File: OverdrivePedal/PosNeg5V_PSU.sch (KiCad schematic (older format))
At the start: 19 parts, among them Q1 DMG2301L, U2 TC7662Bx0A, U3 MIC5233YM5, U4 MIC5270YM5

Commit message: RevA Layout completed
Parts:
- C10, C11, C3, C6, C8: footprint Capacitor_SMD:C_1206_3216Metric_Pad1.42x1.75mm_HandSolder -> Capacitor_SMD:C_0805_2012Metric_Pad1.15x1.40mm_HandSolder
- D1: footprint Diode_SMD:D_SOD-123F -> Diode_SMD:D_SOD-323_HandSoldering
- R4, R5, R6, R7, R8: footprint Resistor_SMD:R_1206_3216Metric_Pad1.42x1.75mm_HandSolder -> Resistor_SMD:R_0805_2012Metric_Pad1.15x1.40mm_HandSolder
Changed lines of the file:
@@
 F 0 "D1" V 3004 2179 50  0000 L CNN
 F 1 "10V" V 3095 2179 50  0000 L CNN
-F 2 "Diode_SMD:D_SOD-123F" H 3050 2100 50  0001 C CNN
+F 2 "Diode_SMD:D_SOD-323_HandSoldering" H 3050 2100 50  0001 C CNN
 F 3 "~" H 3050 2100 50  0001 C CNN
 	1    3050 2100
@@
 F 0 "R4" H 2620 2596 50  0000 L CNN
 F 1 "100K" H 2620 2505 50  0000 L CNN
-F 2 "Resistor_SMD:R_1206_3216Metric_Pad1.42x1.75mm_HandSolder" V 2480 2550 50  0001 C CNN
+F 2 "Resistor_SMD:R_0805_2012Metric_Pad1.15x1.40mm_HandSolder" V 2480 2550 50  0001 C CNN
 F 3 "~" H 2550 2550 50  0001 C CNN
 	1    2550 2550
@@
 F 0 "R7" H 7170 2146 50  0000 L CNN
 F 1 "330R" H 7170 2055 50  0000 L CNN
-F 2 "Resistor_SMD:R_1206_3216Metric_Pad1.42x1.75mm_HandSolder" V 7030 2100 50  0001 C CNN
+F 2 "Resistor_SMD:R_0805_2012Metric_Pad1.15x1.40mm_HandSolder" V 7030 2100 50  0001 C CNN
 F 3 "~" H 7100 2100 50  0001 C CNN
 	1    7100 2100
@@
 F 0 "R5" H 7170 2796 50  0000 L CNN
 F 1 "1K" H 7170 2705 50  0000 L CNN
-F 2 "Resistor_SMD:R_1206_3216Metric_Pad1.42x1.75mm_HandSolder" V 7030 2750 50  0001 C CNN
+F 2 "Resistor_SMD:R_0805_2012Metric_Pad1.15x1.40mm_HandSolder" V 7030 2750 50  0001 C CNN
 F 3 "~" H 7100 2750 50  0001 C CNN
 	1    7100 2750
@@
 F 0 "C6" H 5315 2546 50  0000 L CNN
 F 1 "1uF" H 5315 2455 50  0000 L CNN
-F 2 "Capacitor_SMD:C_1206_3216Metric_Pad1.42x1.75mm_HandSolder" H 5238 2350 50  0001 C CNN
+F 2 "Capacitor_SMD:C_0805_2012Metric_Pad1.15x1.40mm_HandSolder" H 5238 2350 50  0001 C CNN
 F 3 "~" H 5200 2500 50  0001 C CNN
 	1    5200 2500
@@
 F 0 "C8" H 7585 2546 50  0000 R CNN
 F 1 "2.2uF" H 7585 2455 50  0000 R CNN
-F 2 "Capacitor_SMD:C_1206_3216Metric_Pad1.42x1.75mm_HandSolder" H 7738 2350 50  0001 C CNN
+F 2 "Capacitor_SMD:C_0805_2012Metric_Pad1.15x1.40mm_HandSolder" H 7738 2350 50  0001 C CNN
 F 3 "~" H 7700 2500 50  0001 C CNN
 	1    7700 2500
@@
 F 0 "R8" H 7170 4496 50  0000 L CNN
 F 1 "330R" H 7170 4405 50  0000 L CNN
-F 2 "Resistor_SMD:R_1206_3216Metric_Pad1.42x1.75mm_HandSolder" V 7030 4450 50  0001 C CNN
+F 2 "Resistor_SMD:R_0805_2012Metric_Pad1.15x1.40mm_HandSolder" V 7030 4450 50  0001 C CNN
 F 3 "~" H 7100 4450 50  0001 C CNN
 	1    7100 4450
@@
 F 0 "R6" H 7170 5096 50  0000 L CNN
 F 1 "1K" H 7170 5005 50  0000 L CNN
-F 2 "Resistor_SMD:R_1206_3216Metric_Pad1.42x1.75mm_HandSolder" V 7030 5050 50  0001 C CNN
+F 2 "Resistor_SMD:R_0805_2012Metric_Pad1.15x1.40mm_HandSolder" V 7030 5050 50  0001 C CNN
 F 3 "~" H 7100 5050 50  0001 C CNN
 	1    7100 5050
@@
 F 0 "C3" H 1665 4896 50  0000 L CNN
 F 1 "100nF" H 1665 4805 50  0000 L CNN
-F 2 "Capacitor_SMD:C_1206_3216Metric_Pad1.42x1.75mm_HandSolder" H 1588 4700 50  0001 C CNN
+F 2 "Capacitor_SMD:C_0805_2012Metric_Pad1.15x1.40mm_HandSolder" H 1588 4700 50  0001 C CNN
 F 3 "~" H 1550 4850 50  0001 C CNN
 	1    1550 4850
@@
 F 0 "C10" H 9615 2346 50  0000 L CNN
 F 1 "100nF" H 9615 2255 50  0000 L CNN
-F 2 "Capacitor_SMD:C_1206_3216Metric_Pad1.42x1.75mm_HandSolder" H 9538 2150 50  0001 C CNN
+F 2 "Capacitor_SMD:C_0805_2012Metric_Pad1.15x1.40mm_HandSolder" H 9538 2150 50  0001 C CNN
 F 3 "~" H 9500 2300 50  0001 C CNN
 	1    9500 2300
@@
 F 0 "C11" H 9565 4696 50  0000 L CNN
 F 1 "100nF" H 9565 4605 50  0000 L CNN
-F 2 "Capacitor_SMD:C_1206_3216Metric_Pad1.42x1.75mm_HandSolder" H 9488 4500 50  0001 C CNN
+F 2 "Capacitor_SMD:C_0805_2012Metric_Pad1.15x1.40mm_HandSolder" H 9488 4500 50  0001 C CNN
 F 3 "~" H 9450 4650 50  0001 C CNN
 	1    9450 4650

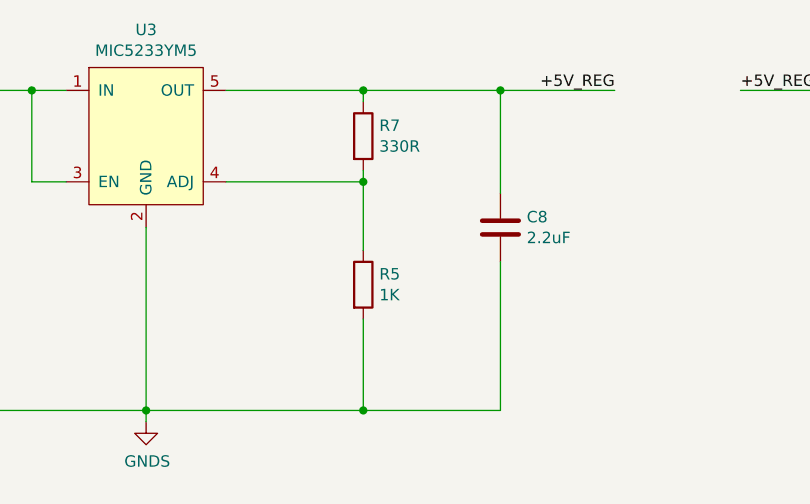
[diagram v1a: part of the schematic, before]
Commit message: Tested RevA Layout
- Removed AC coupling caps
- Reversed Switch connector
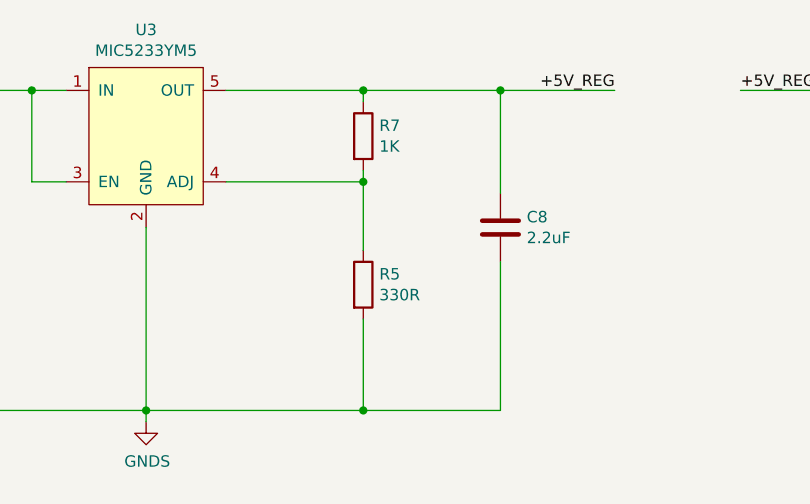
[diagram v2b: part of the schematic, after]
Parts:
- R5: value 1K -> 330R
- R7: value 330R -> 1K
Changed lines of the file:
@@
 AR Path="/5E6A8284/5E61A3C3" Ref="R?"  Part="1"
 F 0 "R7" H 7170 2146 50  0000 L CNN
-F 1 "330R" H 7170 2055 50  0000 L CNN
+F 1 "1K" H 7170 2055 50  0000 L CNN
 F 2 "Resistor_SMD:R_0805_2012Metric_Pad1.15x1.40mm_HandSolder" V 7030 2100 50  0001 C CNN
 F 3 "~" H 7100 2100 50  0001 C CNN
@@
 AR Path="/5E6A8284/5E61A7F8" Ref="R?"  Part="1"
 F 0 "R5" H 7170 2796 50  0000 L CNN
-F 1 "1K" H 7170 2705 50  0000 L CNN
+F 1 "330R" H 7170 2705 50  0000 L CNN
 F 2 "Resistor_SMD:R_0805_2012Metric_Pad1.15x1.40mm_HandSolder" V 7030 2750 50  0001 C CNN
 F 3 "~" H 7100 2750 50  0001 C CNN

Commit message: changed polarity protection mosfet to schotky diode
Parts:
- removed D1: 10V, Diode_SMD:D_SOD-323_HandSoldering, symbol Device:D_Zener
- removed Q1: DMG2301L, Package_TO_SOT_SMD:SOT-23, symbol Transistor_FET:DMG2301L
- removed R4: 100K, Resistor_SMD:R_0805_2012Metric_Pad1.15x1.40mm_HandSolder, symbol Device:R
- added D1: D_Schottky, Diode_SMD:D_SOD-123F, symbol Device:D_Schottky
- U2: symbol Converter_DCDC:TC7662Bx0A -> OverdrivePedal-rescue:TC7662Bx0A-Converter_DCDC
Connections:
- net +9V_IN: now also D1.2 (A)
- net +9V_POL: now also D1.1 (K)
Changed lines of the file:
@@
 $EndDescr
 $Comp
-L Converter_DCDC:TC7662Bx0A U?
+L OverdrivePedal-rescue:TC7662Bx0A-Converter_DCDC U?
 U 1 1 5E618EFD
 P 2450 4500
@@
 	1    0    0    -1
 $EndComp
-$Comp
-L Transistor_FET:DMG2301L Q?
-U 1 1 5E618F03
-P 2550 2000
-AR Path="/5E618F03" Ref="Q?"  Part="1"
-AR Path="/5E6165F4/5E618F03" Ref="Q1"  Part="1"
-AR Path="/5E6A8284/5E618F03" Ref="Q?"  Part="1"
-F 0 "Q1" V 2892 2000 50  0000 C CNN
-F 1 "DMG2301L" V 2801 2000 50  0000 C CNN
-F 2 "Package_TO_SOT_SMD:SOT-23" H 2750 1925 50  0001 L CIN
-F 3 "https://www.diodes.com/assets/Datasheets/DMG2301L.pdf" H 2550 2000 50  0001 L CNN
-	1    2550 2000
-	0    -1   -1   0
-$EndComp
-$Comp
-L Device:D_Zener D?
-U 1 1 5E618F09
-P 3050 2100
-AR Path="/5E618F09" Ref="D?"  Part="1"
-AR Path="/5E6165F4/5E618F09" Ref="D1"  Part="1"
-AR Path="/5E6A8284/5E618F09" Ref="D?"  Part="1"
-F 0 "D1" V 3004 2179 50  0000 L CNN
-F 1 "10V" V 3095 2179 50  0000 L CNN
-F 2 "Diode_SMD:D_SOD-323_HandSoldering" H 3050 2100 50  0001 C CNN
-F 3 "~" H 3050 2100 50  0001 C CNN
-	1    3050 2100
-	0    1    1    0
-$EndComp
-$Comp
-L Device:R R?
-U 1 1 5E618F0F
-P 2550 2550
-AR Path="/5E618F0F" Ref="R?"  Part="1"
-AR Path="/5E6165F4/5E618F0F" Ref="R4"  Part="1"
-AR Path="/5E6A8284/5E618F0F" Ref="R?"  Part="1"
-F 0 "R4" H 2620 2596 50  0000 L CNN
-F 1 "100K" H 2620 2505 50  0000 L CNN
-F 2 "Resistor_SMD:R_0805_2012Metric_Pad1.15x1.40mm_HandSolder" V 2480 2550 50  0001 C CNN
-F 3 "~" H 2550 2550 50  0001 C CNN
-	1    2550 2550
-	1    0    0    -1
-$EndComp
-Wire Wire Line
-	3050 1950 3050 1900
-Wire Wire Line
-	3050 1900 2750 1900
-Wire Wire Line
-	2550 2200 2550 2300
-Wire Wire Line
-	2550 2300 3050 2300
-Wire Wire Line
-	3050 2300 3050 2250
-Connection ~ 2550 2300
-Wire Wire Line
-	2550 2300 2550 2400
-$Comp
-L power:GNDS #PWR?
-U 1 1 5E618F1D
-P 2550 2850
-AR Path="/5E618F1D" Ref="#PWR?"  Part="1"
-AR Path="/5E6165F4/5E618F1D" Ref="#PWR012"  Part="1"
-AR Path="/5E6A8284/5E618F1D" Ref="#PWR?"  Part="1"
-F 0 "#PWR012" H 2550 2600 50  0001 C CNN
-F 1 "GNDS" H 2555 2677 50  0000 C CNN
-F 2 "" H 2550 2850 50  0001 C CNN
-F 3 "" H 2550 2850 50  0001 C CNN
-	1    2550 2850
-	1    0    0    -1
-$EndComp
-Wire Wire Line
-	1350 1900 2350 1900
+Wire Wire Line
+	1350 1900 2450 1900
 Text Label 2000 1900 0    50   ~ 0
 +9V
-Wire Wire Line
-	3050 1900 3750 1900
-Connection ~ 3050 1900
 Text Label 3750 1900 2    50   ~ 0
 +9V_POL
@@
 Text HLabel 1350 1900 0    50   Input ~ 0
 +9V_IN
-Wire Wire Line
-	2550 2700 2550 2750
 Text HLabel 10200 1900 2    50   Input ~ 0
 +5V
@@
 	9450 4250 8700 4250
 $Comp
-L power:PWR_FLAG #FLG0101
-U 1 1 5E6C6F22
-P 3050 1900
-F 0 "#FLG0101" H 3050 1975 50  0001 C CNN
-F 1 "PWR_FLAG" H 3050 2073 50  0000 C CNN
-F 2 "" H 3050 1900 50  0001 C CNN
-F 3 "~" H 3050 1900 50  0001 C CNN
-	1    3050 1900
-	1    0    0    -1
-$EndComp
-$Comp
-L power:PWR_FLAG #FLG0102
-U 1 1 5E6C767F
-P 2950 2850
-F 0 "#FLG0102" H 2950 2925 50  0001 C CNN
-F 1 "PWR_FLAG" H 2950 3023 50  0000 C CNN
-F 2 "" H 2950 2850 50  0001 C CNN
-F 3 "~" H 2950 2850 50  0001 C CNN
-	1    2950 2850
-	-1   0    0    1
-$EndComp
-Wire Wire Line
-	2950 2850 2950 2750
-Wire Wire Line
-	2950 2750 2550 2750
-Connection ~ 2550 2750
-Wire Wire Line
-	2550 2750 2550 2850
-$Comp
 L MIC5233:MIC5233YM5 U3
 U 1 1 5E6DAB67
@@
 	1    0    0    -1
 $EndComp
+$Comp
+L Device:D_Schottky D1
+U 1 1 5F64055A
+P 2600 1900
+F 0 "D1" H 2600 1683 50  0000 C CNN
+F 1 "D_Schottky" H 2600 1774 50  0000 C CNN
+F 2 "Diode_SMD:D_SOD-123F" H 2600 1900 50  0001 C CNN
+F 3 "~" H 2600 1900 50  0001 C CNN
+	1    2600 1900
+	-1   0    0    1
+$EndComp
+Wire Wire Line
+	2750 1900 3175 1900
+$Comp
+L power:PWR_FLAG #FLG0102
+U 1 1 5F65BAE4
+P 3175 1725
+F 0 "#FLG0102" H 3175 1800 50  0001 C CNN
+F 1 "PWR_FLAG" H 3175 1898 50  0000 C CNN
+F 2 "" H 3175 1725 50  0001 C CNN
+F 3 "~" H 3175 1725 50  0001 C CNN
+	1    3175 1725
+	1    0    0    -1
+$EndComp
+Wire Wire Line
+	3175 1725 3175 1900
+Connection ~ 3175 1900
+Wire Wire Line
+	3175 1900 3750 1900
 $EndSCHEMATC

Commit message: updates
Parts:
- removed C4, C5: 10uF, Capacitor_SMD:CP_Elec_4x5.7, symbol Device:CP
- removed U2: TC7662Bx0A, Package_SO:SOIC-8_3.9x4.9mm_P1.27mm, symbol OverdrivePedal-rescue:TC7662Bx0A-Converter_DCDC
- added C?: 1uF, Capacitor_SMD:C_0805_2012Metric_Pad1.15x1.40mm_HandSolder, symbol Device:C
- added U?: TPS60400, Package_TO_SOT_SMD:SOT-23-5_HandSoldering, symbol TPS6040x:TPS60400
- C3: value 100nF -> 1uF
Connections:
- net +9V_POL: now also U?.2 (IN); no longer C3.1
- net -9V_POL: now also C?.1, U?.1 (OUT)
- net GNDS: now also C?.2, U?.4 (GND); no longer C3.2
- new net: C3.1, U?.3 (CFLY-)
- new net: C3.2, U?.5 (CFLY+)
- no-connect marks 3 -> 1
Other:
- moved on the sheet: C3, C6, C8, R5, R7, U3
